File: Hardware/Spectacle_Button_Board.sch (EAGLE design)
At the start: 54 parts, among them J17 AUDIO-JACK3, J20 AUDIO-JACK3, U1 CY8C4146LQI-S422, U2 3.3V/150mA, U4 SN74LVC1G66, U5 SN74LVC1G66

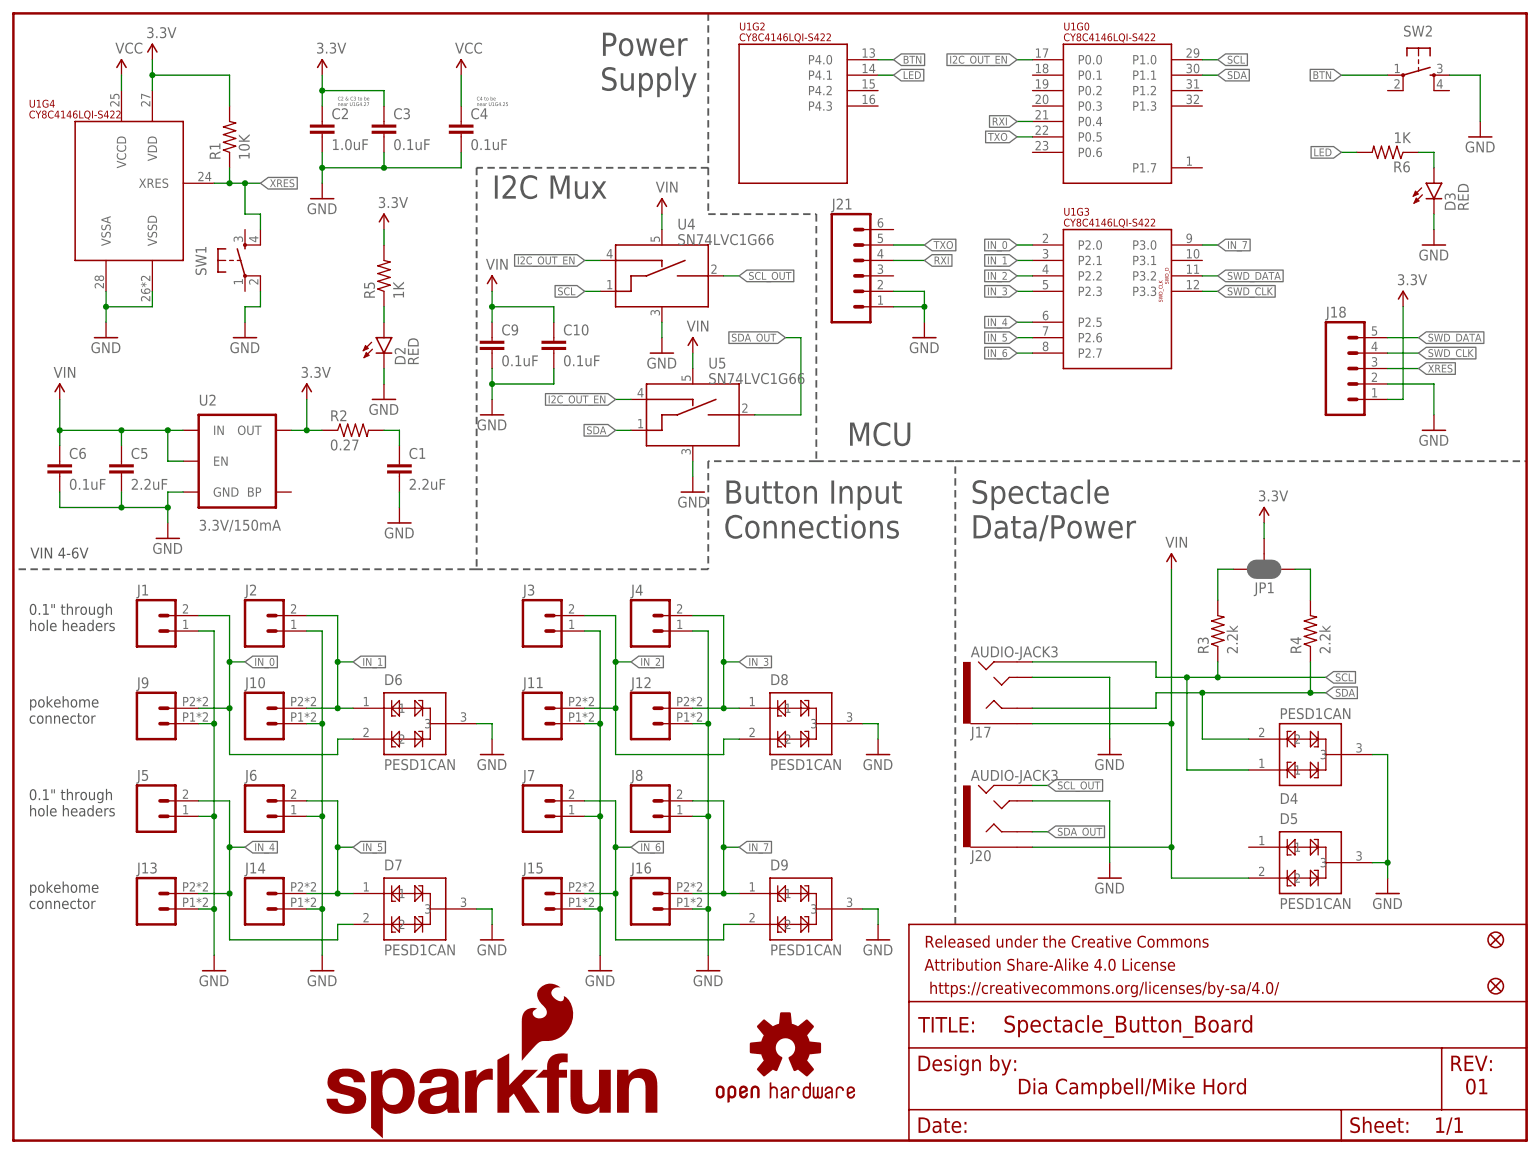
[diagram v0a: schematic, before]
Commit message: Fixes from review and checklist
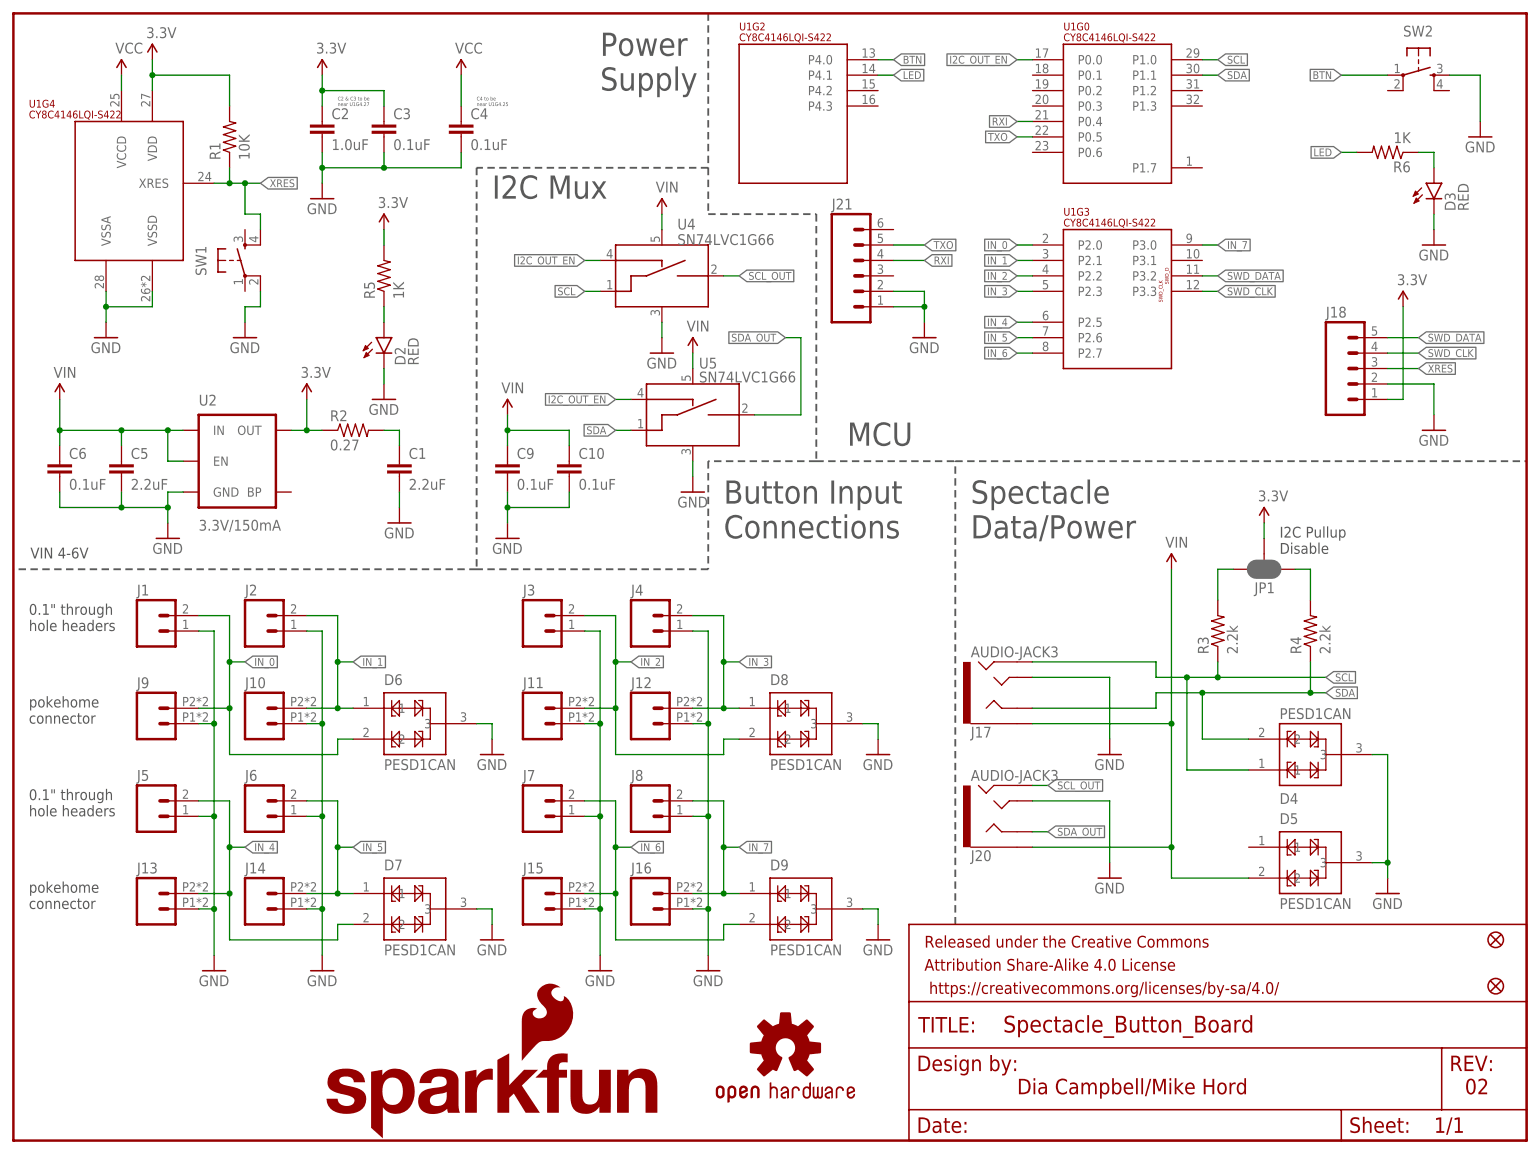
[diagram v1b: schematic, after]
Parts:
- J21: device SparkFun-Connectors:M06NO_SILK_FEMALE_PTH -> SparkFun-Connectors:M06NO_SILK_NO_POP
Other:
- note added: "02"
- note added: "I2C Pullup Disable"
- note removed: "01"
- moved on the sheet: C10, C9
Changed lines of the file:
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@@
 <?xml version="1.0" encoding="utf-8"?>
 <!DOCTYPE eagle SYSTEM "eagle.dtd">
-<eagle version="7.6.0">
+<eagle version="7.7.0">
 <drawing>
 <settings>
@@
 <part name="GND22" library="SparkFun-Aesthetics" deviceset="GND" device=""/>
 <part name="GND23" library="SparkFun-Aesthetics" deviceset="GND" device=""/>
-<part name="J21" library="SparkFun-Connectors" deviceset="M06" device="NO_SILK_FEMALE_PTH"/>
+<part name="J21" library="SparkFun-Connectors" deviceset="M06" device="NO_SILK_NO_POP"/>
 <part name="C9" library="SparkFun-Capacitors" deviceset="0.1UF-16V(+-10%)(0402)" device="" value="0.1uF"/>
 <part name="C10" library="SparkFun-Capacitors" deviceset="0.1UF-16V(+-10%)(0402)" device="" value="0.1uF"/>
@@
 Supply</text>
 <text x="165.1" y="7.62" size="2.54" layer="94">Dia Campbell/Mike Hord</text>
-<text x="238.76" y="7.62" size="2.54" layer="94">01</text>
+<text x="238.76" y="7.62" size="2.54" layer="94">02</text>
 <text x="2.794" y="95.758" size="1.778" layer="97">VIN 4-6V</text>
 <text x="2.54" y="38.1" size="1.778" layer="97">pokehome
@@
 <wire x1="76.2" y1="160.02" x2="76.2" y2="93.98" width="0.3048" layer="97" style="longdash"/>
 <text x="78.74" y="154.94" size="3.81" layer="97">I2C Mux</text>
+<text x="208.28" y="96.52" size="1.778" layer="97">I2C Pullup
+Disable</text>
 </plain>
 <instances>
@@
 <instance part="FD2" gate="G$1" x="243.84" y="25.4"/>
 <instance part="U4" gate="G$1" x="99.06" y="137.16"/>
-<instance part="U5" gate="G$1" x="104.14" y="114.3"/>
+<instance part="U5" gate="G$1" x="104.14" y="114.3" smashed="yes">
+<attribute name="NAME" x="112.776" y="127" size="1.778" layer="95"/>
+<attribute name="VALUE" x="112.776" y="124.714" size="1.778" layer="96"/>
+</instance>
 <instance part="SUPPLY10" gate="G$1" x="106.68" y="152.4"/>
 <instance part="SUPPLY16" gate="G$1" x="111.76" y="129.54"/>
@@
 <instance part="GND23" gate="1" x="111.76" y="106.68"/>
 <instance part="J21" gate="G$1" x="139.7" y="142.24"/>
-<instance part="C9" gate="G$1" x="78.74" y="129.54"/>
-<instance part="C10" gate="G$1" x="88.9" y="129.54"/>
-<instance part="GND24" gate="1" x="78.74" y="119.38"/>
-<instance part="SUPPLY17" gate="G$1" x="78.74" y="139.7"/>
+<instance part="C9" gate="G$1" x="81.28" y="109.22"/>
+<instance part="C10" gate="G$1" x="91.44" y="109.22"/>
+<instance part="GND24" gate="1" x="81.28" y="99.06"/>
+<instance part="SUPPLY17" gate="G$1" x="81.28" y="119.38"/>
 </instances>
 <busses>
@@
 <pinref part="GND24" gate="1" pin="GND"/>
 <pinref part="C9" gate="G$1" pin="2"/>
-<wire x1="78.74" y1="121.92" x2="78.74" y2="124.46" width="0.1524" layer="91"/>
+<wire x1="81.28" y1="101.6" x2="81.28" y2="104.14" width="0.1524" layer="91"/>
 <pinref part="C10" gate="G$1" pin="2"/>
-<wire x1="78.74" y1="124.46" x2="78.74" y2="127" width="0.1524" layer="91"/>
-<wire x1="78.74" y1="124.46" x2="88.9" y2="124.46" width="0.1524" layer="91"/>
-<wire x1="88.9" y1="124.46" x2="88.9" y2="127" width="0.1524" layer="91"/>
-<junction x="78.74" y="124.46"/>
+<wire x1="81.28" y1="104.14" x2="81.28" y2="106.68" width="0.1524" layer="91"/>
+<wire x1="81.28" y1="104.14" x2="91.44" y2="104.14" width="0.1524" layer="91"/>
+<wire x1="91.44" y1="104.14" x2="91.44" y2="106.68" width="0.1524" layer="91"/>
+<junction x="81.28" y="104.14"/>
 </segment>
 <segment>
@@
 <pinref part="SUPPLY17" gate="G$1" pin="VIN"/>
 <pinref part="C9" gate="G$1" pin="1"/>
-<wire x1="78.74" y1="139.7" x2="78.74" y2="137.16" width="0.1524" layer="91"/>
+<wire x1="81.28" y1="119.38" x2="81.28" y2="116.84" width="0.1524" layer="91"/>
 <pinref part="C10" gate="G$1" pin="1"/>
-<wire x1="78.74" y1="137.16" x2="78.74" y2="134.62" width="0.1524" layer="91"/>
-<wire x1="78.74" y1="137.16" x2="88.9" y2="137.16" width="0.1524" layer="91"/>
-<wire x1="88.9" y1="137.16" x2="88.9" y2="134.62" width="0.1524" layer="91"/>
-<junction x="78.74" y="137.16"/>
-</segment>
-</net>
+<wire x1="81.28" y1="116.84" x2="81.28" y2="114.3" width="0.1524" layer="91"/>
+<wire x1="81.28" y1="116.84" x2="91.44" y2="116.84" width="0.1524" layer="91"/>
+<wire x1="91.44" y1="116.84" x2="91.44" y2="114.3" width="0.1524" layer="91"/>
+<junction x="81.28" y="116.84"/>
+</segment>
+</net>

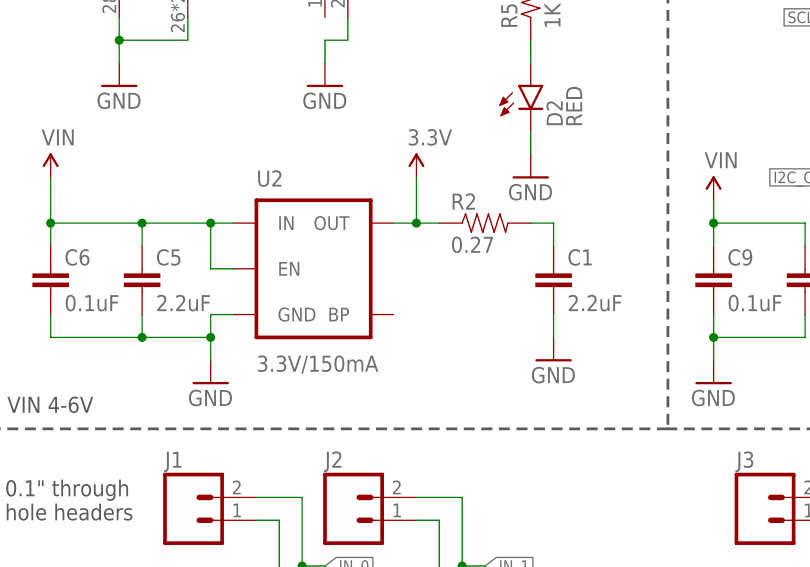
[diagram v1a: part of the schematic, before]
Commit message: Chg VREG to APK2112
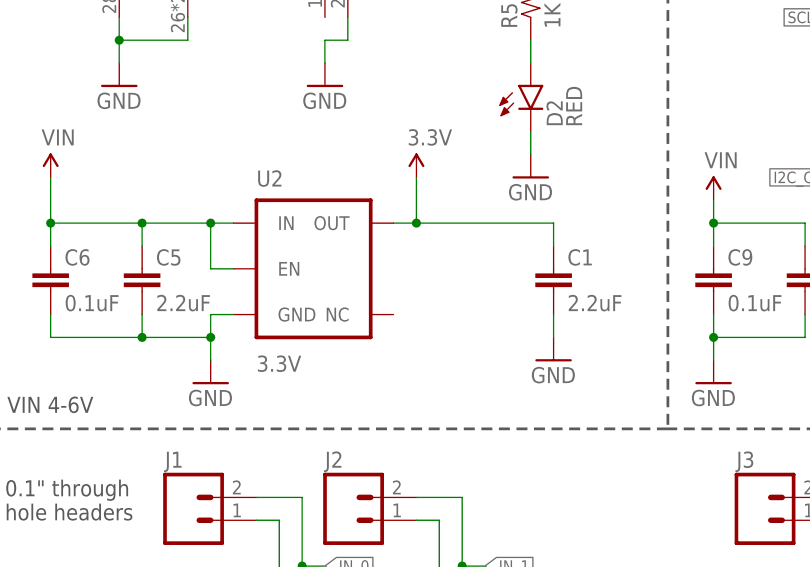
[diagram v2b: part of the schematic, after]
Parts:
- removed R2: 0.27, SparkFun-Resistors:0.27OHM-1/10W-1%(0603)
- U2: value 3.3V/150mA -> 3.3V; device SparkFun-PowerIC:V_REG_MIC52053.3V -> SparkFun-PowerIC:V_REG_AP2112K-3.3V
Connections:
- removed net N$3: C1.1, R2.2
- net 3.3V: now also C1.1; no longer R2.1
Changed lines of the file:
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@@
 <part name="GND1" library="SparkFun-Aesthetics" deviceset="GND" device=""/>
 <part name="SUPPLY2" library="SparkFun-Aesthetics" deviceset="VIN" device=""/>
-<part name="U2" library="SparkFun-PowerIC" deviceset="V_REG_MIC5205" device="3.3V" value="3.3V/150mA"/>
+<part name="U2" library="SparkFun-PowerIC" deviceset="V_REG_AP2112" device="K-3.3V" value="3.3V"/>
 <part name="J1" library="SparkFun-Connectors" deviceset="M02" device="PTH"/>
 <part name="J2" library="SparkFun-Connectors" deviceset="M02" device="PTH"/>
@@
 <part name="R1" library="SparkFun-Resistors" deviceset="10KOHM-1/10W-1%(0603)" device="0603" value="10K"/>
 <part name="GND7" library="SparkFun-Aesthetics" deviceset="GND" device=""/>
-<part name="R2" library="SparkFun-Resistors" deviceset="0.27OHM-1/10W-1%(0603)" device="" value="0.27"/>
 <part name="C1" library="SparkFun-Capacitors" deviceset="2.2UF-10V-20%(0603)" device="" value="2.2uF"/>
 <part name="C2" library="SparkFun-Capacitors" deviceset="1.0UF-16V-10%(0402)" device="" value="1.0uF"/>
@@
 <instance part="GND1" gate="1" x="25.4" y="99.06"/>
 <instance part="SUPPLY2" gate="G$1" x="7.62" y="121.92"/>
-<instance part="U2" gate="U1" x="38.1" y="111.76"/>
+<instance part="U2" gate="G$1" x="38.1" y="111.76"/>
 <instance part="J1" gate="G$1" x="22.86" y="83.82"/>
 <instance part="J2" gate="G$1" x="40.64" y="83.82"/>
@@
 <instance part="R1" gate="G$1" x="35.56" y="165.1" rot="R90"/>
 <instance part="GND7" gate="1" x="63.5" y="101.6"/>
-<instance part="R2" gate="G$1" x="55.88" y="116.84"/>
 <instance part="C1" gate="G$1" x="63.5" y="109.22"/>
 <instance part="C2" gate="G$1" x="50.8" y="165.1"/>
@@
 </segment>
 <segment>
-<pinref part="U2" gate="U1" pin="GND"/>
+<pinref part="U2" gate="G$1" pin="GND"/>
 <pinref part="GND1" gate="1" pin="GND"/>
 <wire x1="27.94" y1="106.68" x2="25.4" y2="106.68" width="0.1524" layer="91"/>
@@
 </segment>
 </net>
-<net name="N$3" class="0">
-<segment>
-<pinref part="R2" gate="G$1" pin="2"/>
-<wire x1="60.96" y1="116.84" x2="63.5" y2="116.84" width="0.1524" layer="91"/>
-<pinref part="C1" gate="G$1" pin="1"/>
-<wire x1="63.5" y1="116.84" x2="63.5" y2="114.3" width="0.1524" layer="91"/>
-</segment>
-</net>
 <net name="VIN" class="0">
 <segment>
-<pinref part="U2" gate="U1" pin="EN"/>
+<pinref part="U2" gate="G$1" pin="EN"/>
 <wire x1="27.94" y1="111.76" x2="25.4" y2="111.76" width="0.1524" layer="91"/>
 <wire x1="25.4" y1="111.76" x2="25.4" y2="116.84" width="0.1524" layer="91"/>
-<pinref part="U2" gate="U1" pin="IN"/>
+<pinref part="U2" gate="G$1" pin="IN"/>
 <wire x1="27.94" y1="116.84" x2="25.4" y2="116.84" width="0.1524" layer="91"/>
 <junction x="25.4" y="116.84"/>
@@
 </segment>
 <segment>
-<pinref part="U2" gate="U1" pin="OUT"/>
+<pinref part="U2" gate="G$1" pin="OUT"/>
 <wire x1="45.72" y1="116.84" x2="48.26" y2="116.84" width="0.1524" layer="91"/>
 <wire x1="48.26" y1="116.84" x2="48.26" y2="121.92" width="0.1524" layer="91"/>
-<pinref part="R2" gate="G$1" pin="1"/>
-<wire x1="48.26" y1="116.84" x2="50.8" y2="116.84" width="0.1524" layer="91"/>
 <junction x="48.26" y="116.84"/>
 <pinref part="SUPPLY12" gate="G$1" pin="3.3V"/>
-</segment>
-<segment>
+<pinref part="C1" gate="G$1" pin="1"/>
+<wire x1="63.5" y1="116.84" x2="63.5" y2="114.3" width="0.1524" layer="91"/>
+<wire x1="48.26" y1="116.84" x2="63.5" y2="116.84" width="0.1524" layer="91"/>
+</segment>
+<segment>

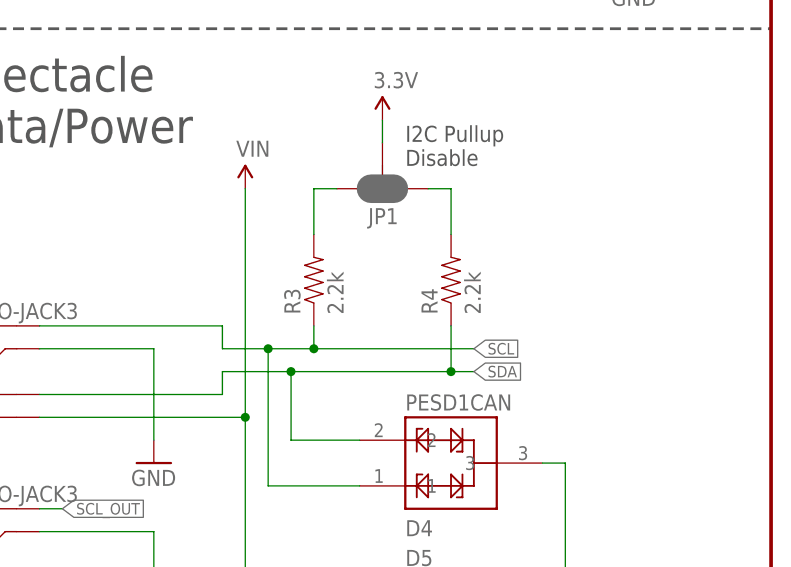
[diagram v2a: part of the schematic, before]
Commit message: Change pullups to 4.7k
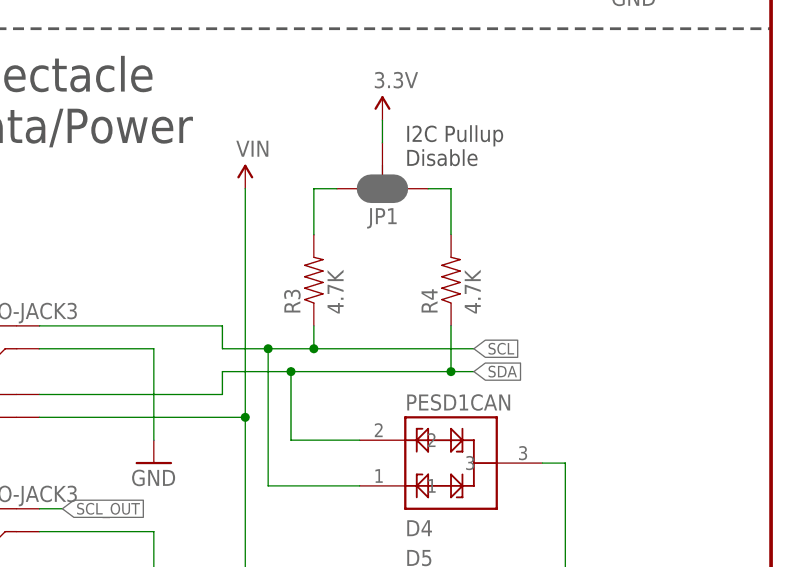
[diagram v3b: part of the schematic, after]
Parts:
- R3, R4: value 2.2k -> 4.7K; device SparkFun-Resistors:2.2KOHM-1/10W-1%(0603) -> SparkFun-Resistors:4.7KOHM-1/10W-1%(0603)
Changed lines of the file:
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@@
 <part name="GND9" library="SparkFun-Aesthetics" deviceset="GND" device=""/>
 <part name="SUPPLY7" library="SparkFun-Aesthetics" deviceset="VIN" device=""/>
-<part name="R3" library="SparkFun-Resistors" deviceset="2.2KOHM-1/10W-1%(0603)" device="" value="2.2k"/>
-<part name="R4" library="SparkFun-Resistors" deviceset="2.2KOHM-1/10W-1%(0603)" device="" value="2.2k"/>
+<part name="R3" library="SparkFun-Resistors" deviceset="4.7KOHM-1/10W-1%(0603)" device="" value="4.7K"/>
+<part name="R4" library="SparkFun-Resistors" deviceset="4.7KOHM-1/10W-1%(0603)" device="" value="4.7K"/>
 <part name="JP1" library="SparkFun-Passives" deviceset="JUMPER-PAD-3-NC_BY_PASTE" device=""/>
 <part name="J18" library="SparkFun-Connectors" deviceset="M05" device="NO_SILK"/>

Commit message: Version number update!
v10
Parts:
- J17, J20: value AUDIO-JACK3 -> AUDIO_JACK_TRRSSMD_RA; device SparkFun-Connectors:AUDIO-JACK3 -> SparkFun-Connectors:AUDIO_JACK_TRRSSMD_RA
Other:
- note added: "10"
- note removed: "02"
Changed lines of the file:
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@@
 <?xml version="1.0" encoding="utf-8"?>
 <!DOCTYPE eagle SYSTEM "eagle.dtd">
-<eagle version="7.7.0">
+<eagle version="7.6.0">
 <drawing>
 <settings>
@@
 <part name="R6" library="SparkFun-Resistors" deviceset="1KOHM-1/10W-1%(0603)" device="" value="1K"/>
 <part name="GND15" library="SparkFun-Aesthetics" deviceset="GND" device=""/>
-<part name="J17" library="SparkFun-Connectors" deviceset="AUDIO-JACK3" device=""/>
+<part name="J17" library="SparkFun-Connectors" deviceset="AUDIO_JACK_TRRS" device="SMD_RA"/>
 <part name="D4" library="SparkFun-DiscreteSemi" deviceset="PESD1CAN" device=""/>
 <part name="D5" library="SparkFun-DiscreteSemi" deviceset="PESD1CAN" device=""/>
@@
 <part name="SUPPLY13" library="SparkFun-Aesthetics" deviceset="3.3V" device=""/>
 <part name="SUPPLY14" library="SparkFun-Aesthetics" deviceset="3.3V" device=""/>
-<part name="J20" library="SparkFun-Connectors" deviceset="AUDIO-JACK3" device=""/>
+<part name="J20" library="SparkFun-Connectors" deviceset="AUDIO_JACK_TRRS" device="SMD_RA"/>
 <part name="GND21" library="SparkFun-Aesthetics" deviceset="GND" device=""/>
 <part name="LOGO1" library="SparkFun-Aesthetics" deviceset="OSHW-LOGO" device="M"/>
@@
 Supply</text>
 <text x="165.1" y="7.62" size="2.54" layer="94">Dia Campbell/Mike Hord</text>
-<text x="238.76" y="7.62" size="2.54" layer="94">02</text>
+<text x="238.76" y="7.62" size="2.54" layer="94">10</text>
 <text x="2.794" y="95.758" size="1.778" layer="97">VIN 4-6V</text>
 <text x="2.54" y="38.1" size="1.778" layer="97">pokehome

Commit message: added v to version number
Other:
- note added: "v10"
- note removed: "10"
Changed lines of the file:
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@@
 Supply</text>
 <text x="165.1" y="7.62" size="2.54" layer="94">Dia Campbell/Mike Hord</text>
-<text x="238.76" y="7.62" size="2.54" layer="94">10</text>
+<text x="238.76" y="7.62" size="2.54" layer="94">v10</text>
 <text x="2.794" y="95.758" size="1.778" layer="97">VIN 4-6V</text>
 <text x="2.54" y="38.1" size="1.778" layer="97">pokehome
